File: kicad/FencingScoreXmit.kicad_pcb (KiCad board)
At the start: 2 copper layers, 35 x 30 mm, 11 parts, among them IC1 PIC16F18323-I/JQ, J1 PWR_IN, J2 SCORE_MACH, U1 MCP1824S33/DB

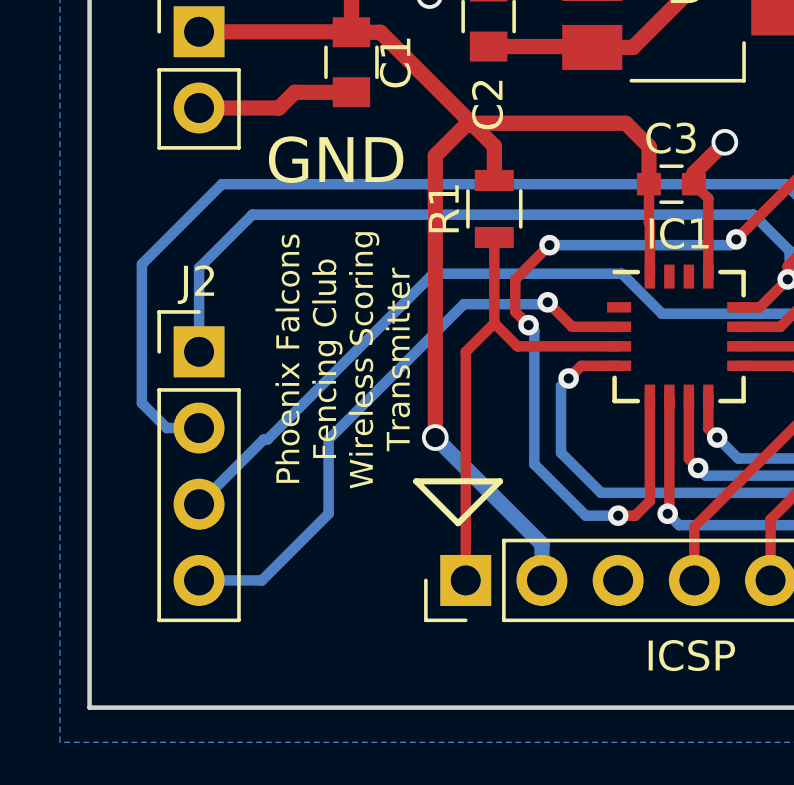
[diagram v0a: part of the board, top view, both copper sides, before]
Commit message: Update RF addr and silkscreen, update for KiCad 7
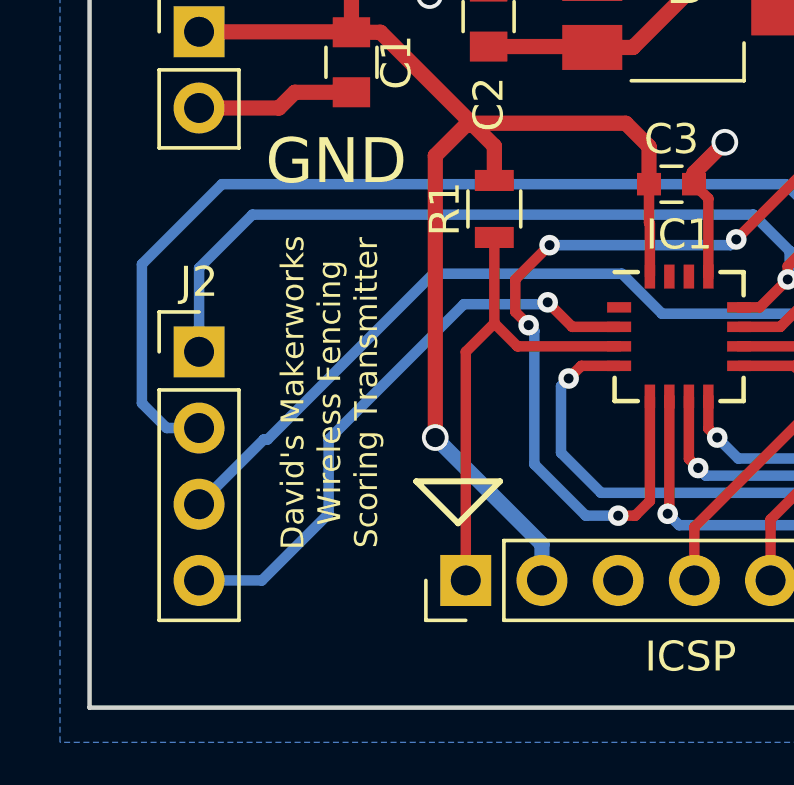
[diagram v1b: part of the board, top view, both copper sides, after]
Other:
- net class Default removed
- board text added: "David's Makerworks Wireless Fencing Scoring Transmitter"
- board text removed: "Phoenix Falcons Fencing Club Wireless Scoring Transmitter"
